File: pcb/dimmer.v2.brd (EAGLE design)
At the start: 69.5 x 90.3 mm, 45 parts, among them M328 ATMEGA328P-AU, SW1 RJ45SMD, SW2 RJ45SMD, SW3 RJ45SMD, T1 IRFR5305, T2 BC847BSMD, T3 BC847BSMD, X1 CSM-7X-DU

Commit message: add web
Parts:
- removed C4, C5: (no value), rcl:C0805
- removed R2: 10k, rcl:R1206
- removed X1: CSM-7X-DU, crystal:CSM-7X-DU
- removed X2: (no value), sparkfun:CRYSTAL-SMD-5X3
- added I2C_BUS1: RJ45SMD, con-tycoelectronics:RJ45SMD
- moved R1 40.0 mm to (33.7, 39.1), turned to 90 degrees
- moved D1 19.5 mm to (27.0, 77.2), turned to 270 degrees
- moved C1 13.6 mm to (41.4, 76.5), turned to 90 degrees
- moved R5 10.6 mm to (51.9, 59.2)
- moved PROG 6.29 mm to (47.6, 69.4), turned to 90 degrees
- moved R14 5.87 mm to (26.7, 65.1)
- moved LED1 5.43 mm to (44.9, 62.9)
- moved R11 4.39 mm to (31.0, 37.3)
- moved R15 4.34 mm to (26.7, 59.5)
- moved R3 3.84 mm to (46.0, 59.4)
- moved R7 3.33 mm to (51.9, 52.5)
- moved R13 3.07 mm to (40.5, 64.3)
- moved 485 2.66 mm to (46.0, 53.2)
- moved I2C 2.43 mm to (34.9, 66.4)
- moved L1117 2.06 mm to (34.8, 77.8)
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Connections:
- net +12V: now also I2C_BUS1.P$1, I2C_BUS1.P$2; no longer C1.+
- net GND: now also I2C_BUS1.P$3, I2C_BUS1.P$4, I2C_BUS1.P$5; no longer C4.1, C5.1
- net IN: now also C1.+; no longer R2.2
- net LX: now also I2C_BUS1.P$8
- net LY: now also I2C_BUS1.P$6
- net N$26: no longer R2.1
- net N$49: no longer C4.2, X1.2, X2.3
- net N$50: no longer C5.2, X1.1, X2.1
- net VCC: now also I2C_BUS.P$7, I2C_BUS1.P$7
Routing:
- net N$26: track 78.1 -> 0.00 mm, vias 2 -> 0
- net LY: track 4.56 -> 50.2 mm, vias 0 -> 2
- net LX: track 7.61 -> 44.0 mm, vias 0 -> 2
- net GND: track 126.5 -> 157.0 mm
- net VCC: track 133.8 -> 159.4 mm
- net N$50: track 24.2 -> 0.00 mm
- net IN: track 40.9 -> 19.6 mm
- net N$49: track 21.2 -> 0.00 mm
- net N$4: track 14.5 -> 0.00 mm, vias 2 -> 0
- net N$5: track 15.6 -> 2.07 mm, vias 2 -> 1
- net N$33: track 16.2 -> 3.86 mm
- net N$6: track 28.1 -> 18.4 mm
- net N$17: track 8.35 -> 0.00 mm
- net N$23: track 7.83 -> 0.00 mm
- net N$29: track 9.41 -> 17.2 mm
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
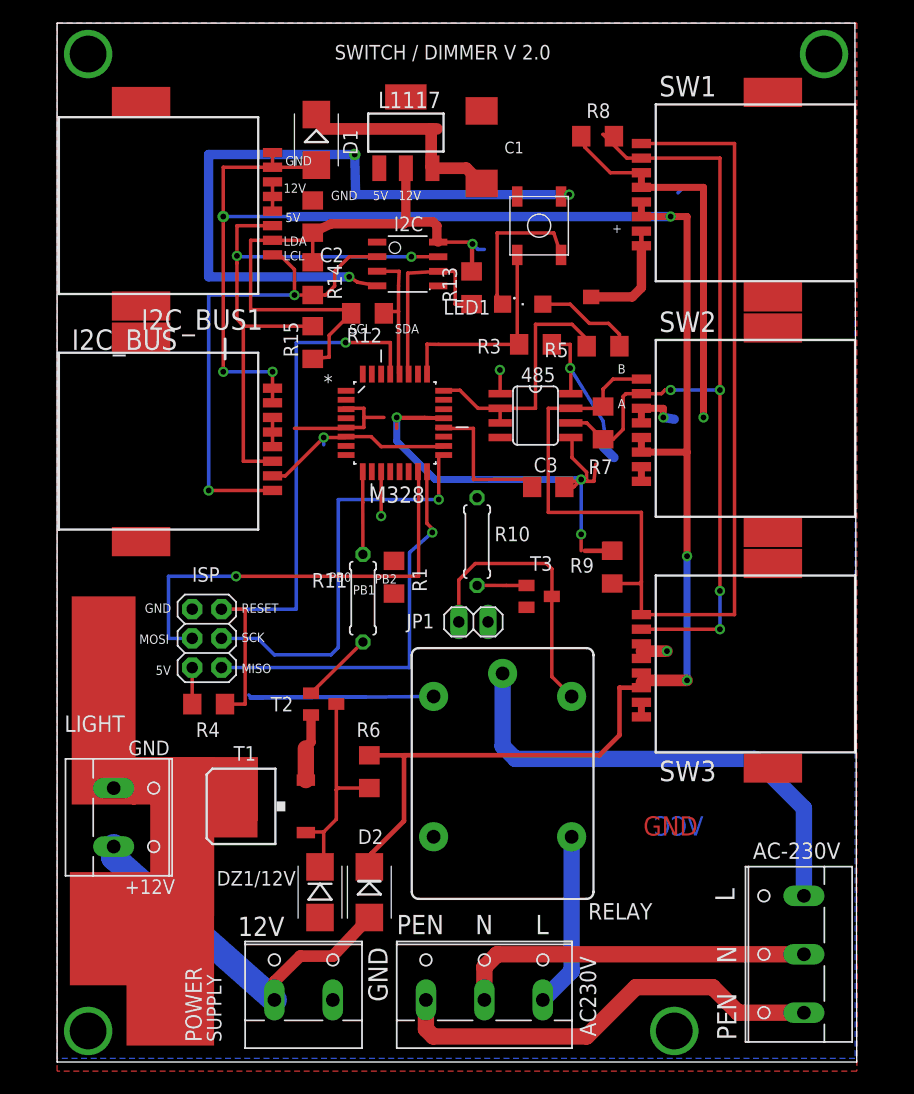
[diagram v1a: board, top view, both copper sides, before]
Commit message: add booster
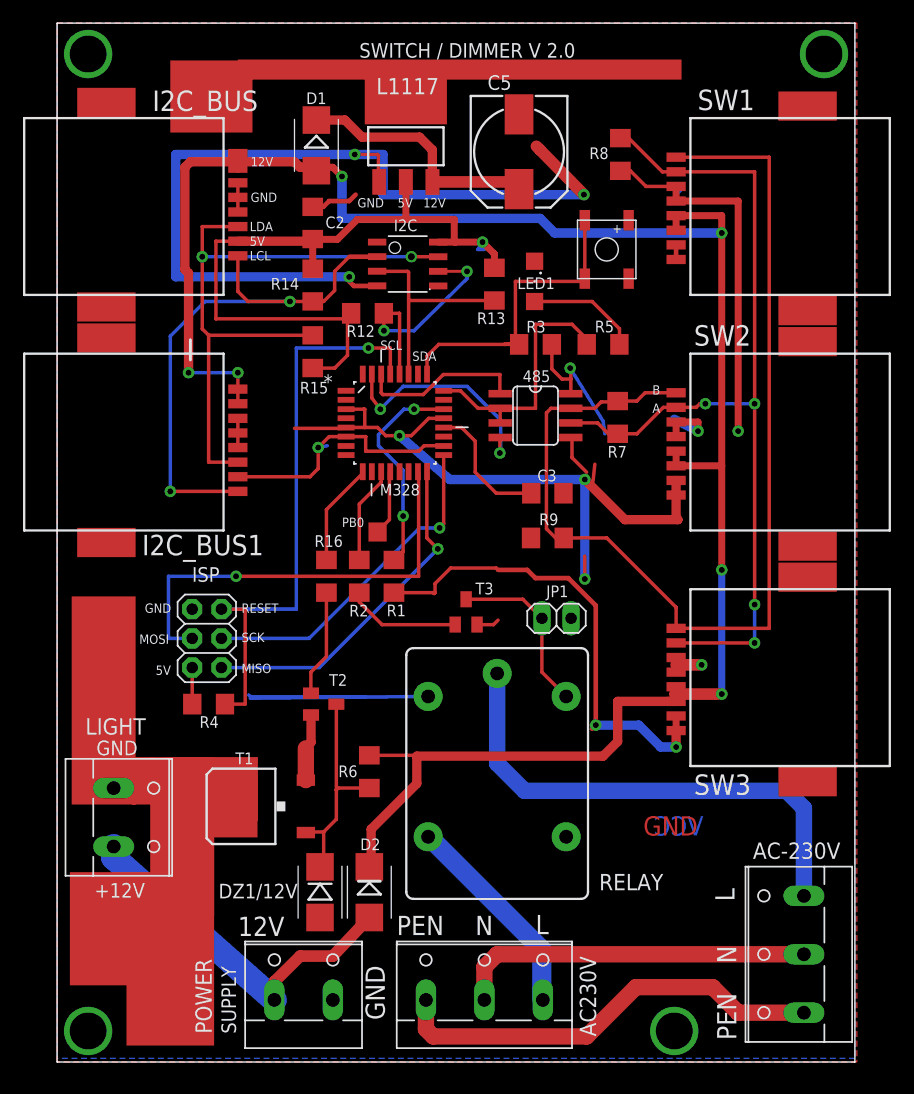
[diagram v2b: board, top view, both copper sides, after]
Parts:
- removed C1: (no value), rcl:SMC_D
- removed R10, R11: (no value), rcl:0207/7
- added C5: 100uF, rcl:140CLH-0810
- added R16, R2: 680, rcl:R1206
- moved JP1 7.23 mm to (47.9, 35.6)
- moved T3 6.49 mm to (40.0, 36.1), turned to 0 degrees
- moved PROG 6.23 mm to (53.5, 67.3)
- moved R9 6.18 mm to (47.1, 42.5), turned to 0 degrees
- moved SW2 3.24 mm to (66.5, 50.7)
- moved SW3 3.24 mm to (66.5, 30.2)
- moved SW1 3.24 mm to (66.5, 71.2)
- moved I2C_BUS 3.02 mm to (11.9, 71.5)
- moved I2C_BUS1 3.02 mm to (11.9, 51.0)
- moved R8 2.54 mm to (53.4, 75.9), turned to 270 degrees
- moved LED1 2.24 mm to (46.0, 64.8), turned to 270 degrees
- moved R13 2.01 mm to (42.5, 64.6)
- moved R7 1.36 mm to (53.2, 53.0)
- moved L1117 1.19 mm to (34.8, 76.6)
- moved R15 0.79 mm to (26.7, 58.7)
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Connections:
- removed net N$14: AC230V.3, RELAY.NC
- removed net N$28: I2C.3, M328.28, R12.1
- removed net N$29: I2C.6, M328.27, R13.1
- new net N$8: AC230V.3, RELAY.NO
- new net SCL: I2C.6, M328.28, R12.1
- new net SDA: I2C.3, M328.27, R13.1
- net GND: now also C5.-; no longer C1.-
- net IN: now also C5.+; no longer C1.+
- net N$13: now also R2.2; no longer R10.1
- net N$2: now also R16.1; no longer R11.2
- net N$33: now also R2.1; no longer R10.2
- net N$7: now also R16.2; no longer R11.1
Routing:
- net GND: track 157.0 -> 203.1 mm, vias 6 -> 8
- net SCL: track 0.00 -> 20.4 mm, vias 0 -> 2
- net N$4: track 0.00 -> 20.1 mm, vias 0 -> 2
- net SDA: track 0.00 -> 19.1 mm
- net N$26: track 0.00 -> 18.7 mm, vias 0 -> 2
- net N$8: track 0.00 -> 18.4 mm
- net N$29: track 17.2 -> 0.00 mm
- net N$14: track 15.2 -> 0.00 mm
- net N$5: track 2.07 -> 14.4 mm, vias 1 -> 0
- net N$28: track 12.2 -> 0.00 mm
- net VCC: track 159.4 -> 170.2 mm
- net N$41: track 24.3 -> 14.9 mm
- net +12V: track 169.7 -> 178.9 mm
- net N$6: track 18.4 -> 27.6 mm
- net SCK: track 36.9 -> 29.4 mm
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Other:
- board size 69.5 x 90.3 mm -> 69.4 x 90.3 mm
- board text added: "Raspberry PI I2C expander board"
- board text added: "switching power supply"
- board text added: "wall switch"
- board text removed: "PB1"
- board text removed: "PB2"

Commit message: add socket io
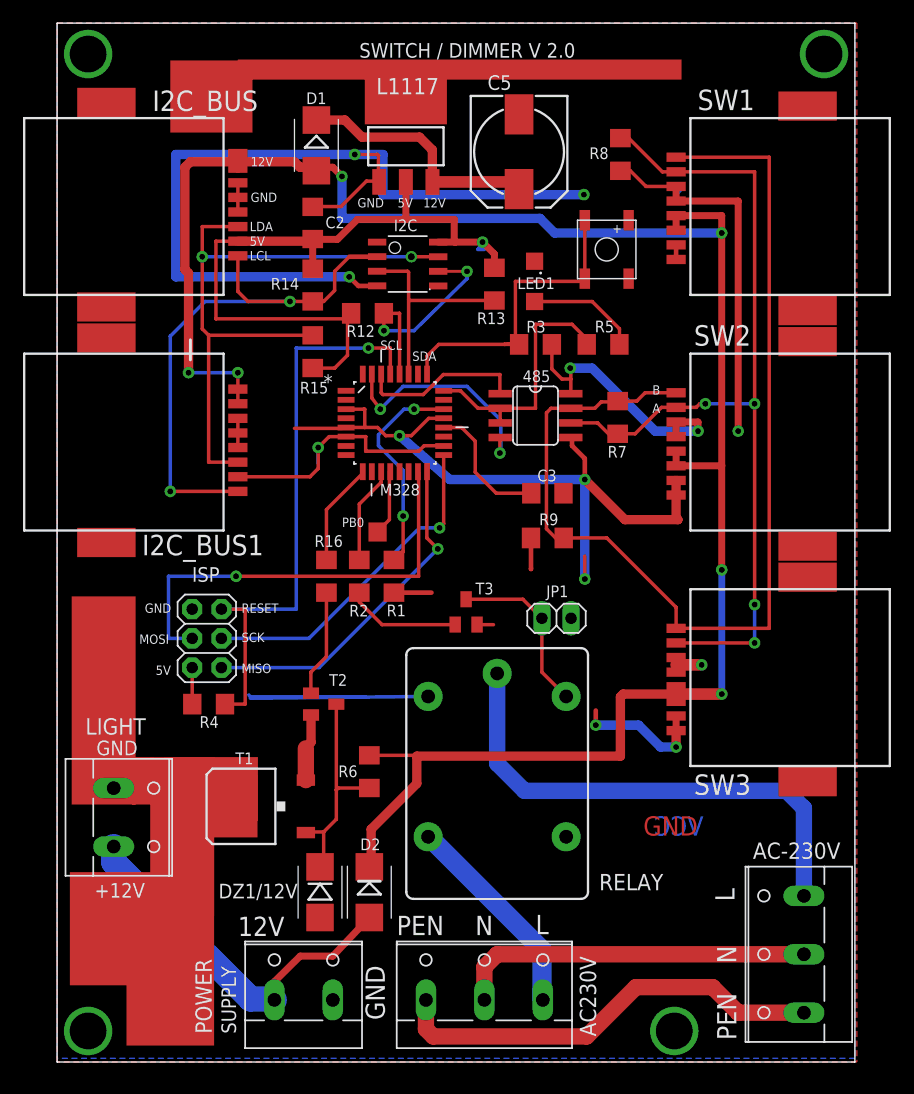
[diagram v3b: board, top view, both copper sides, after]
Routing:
- net GND: track 203.1 -> 174.4 mm
- net VCC: track 170.2 -> 175.4 mm
- net +12V: track 178.9 -> 180.1 mm
- net 12V: track 31.8 -> 32.5 mm
